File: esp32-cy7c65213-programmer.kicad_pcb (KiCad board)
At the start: 2 copper layers, 69.7 x 22.9 mm, 25 parts, among them J1 USB_C, J2 Conn_01x07, Q1 2N3904, Q2 2N3904, U1 TLV1117-33, U2 CY7C65213-28PVXI

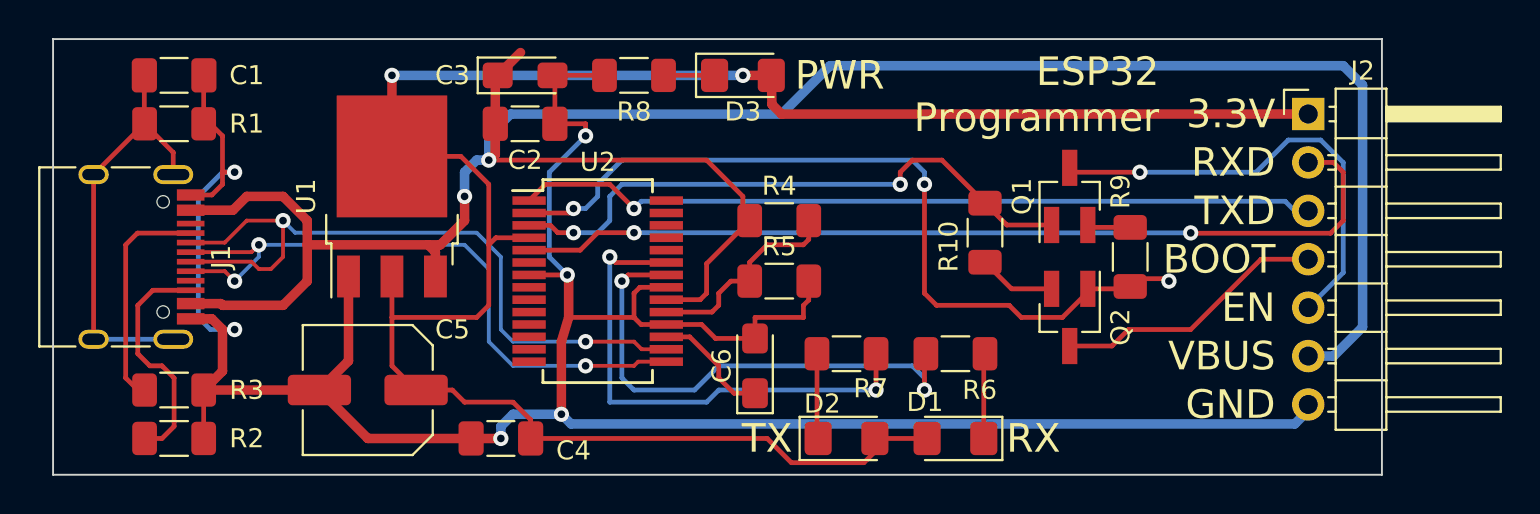
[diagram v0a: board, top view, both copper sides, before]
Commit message: Fix wrong transistor type and update the screenshots
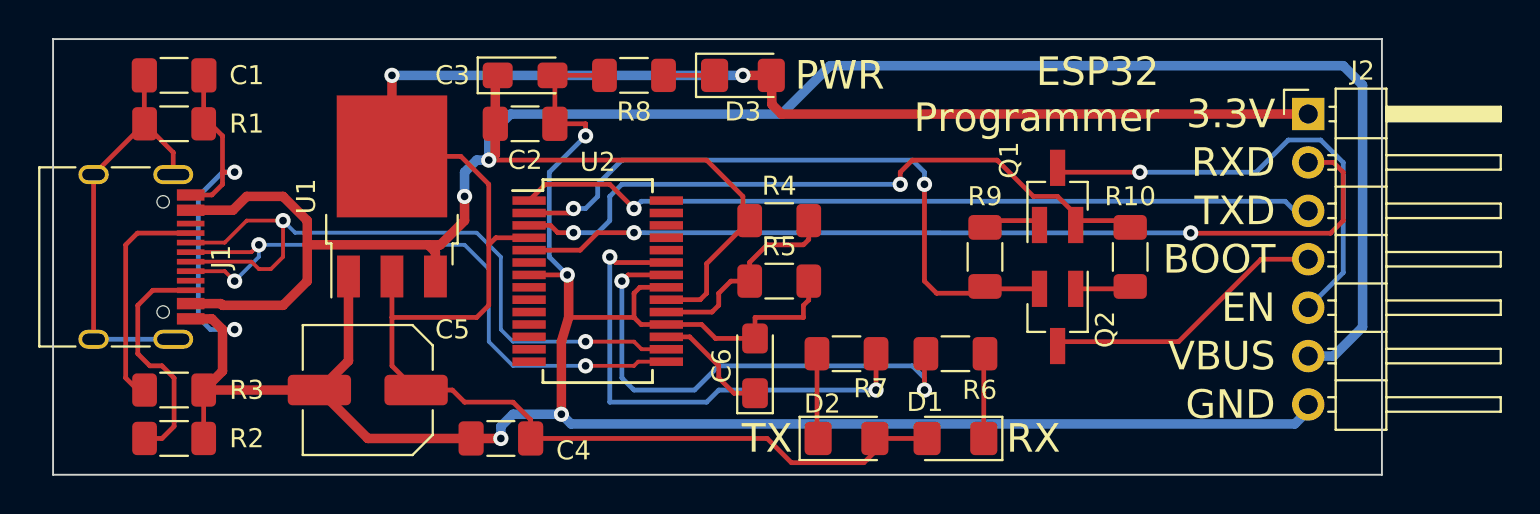
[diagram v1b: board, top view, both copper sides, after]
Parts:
- Q1, Q2: value 2N3904 -> BC847
- moved R10 7.73 mm to (147.3, 108.6)
- moved R9 7.62 mm to (139.7, 108.6)
- moved Q1 0.64 mm to (143.5, 105.4)
- moved Q2 0.64 mm to (143.5, 111.8)
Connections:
- Q1 pad 1: RTS -> Net-(R9-Pad2)
- Q1 pad 2: Net-(Q1-Pad2) -> RTS
- Q2 pad 1: DTR -> Net-(R10-Pad2)
- Q2 pad 2: Net-(R10-Pad2) -> DTR
- R9 pad 2: Net-(Q1-Pad2) -> Net-(R9-Pad2)
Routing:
- net DTR: track 43.5 -> 34.7 mm, vias 3 -> 2
- net RTS: track 31.7 -> 36.4 mm
- net Net-(R9-Pad2): track 0.00 -> 3.10 mm
- net Net-(Q1-Pad2): track 2.28 -> 0.00 mm
- net VBUS: track 126.1 -> 124.4 mm
- net Net-(R10-Pad2): track 4.07 -> 3.32 mm
- net BOOT: track 14.4 -> 15.0 mm
- net EN: track 24.3 -> 24.8 mm
